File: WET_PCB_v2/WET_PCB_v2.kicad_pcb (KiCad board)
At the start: 2 copper layers, 100 x 80 mm, 185 parts, among them J1 Barrel jack, J10 POGO1, J11 Conn_01x09_Pin, J12 Conn_01x09_Pin, J13 Capacitor connector, J14 Capacitor connector, J15 Capacitor connector, J16 Capacitor connector, J17 Capacitor connector, J18 Capacitor connector, J2 Power input, J3 Jumper, J31 LA55_GND, J32 LA55_+, J33 LA55_M, J34 Capacitor connector, J35 PRGM_DBG, J36 LED_POWER, J37 PRGM_DBG, J39 TEST, J4 Coil plug, J40 TEST, J41 TEST, J43 PRGM_DBG, J44 GND, J45 PRGM_DBG, J46 GND, J47 GND, J5 Vsense_ADC1_IN1, J6 Pluggable Terminal Block, J7 Conn_01x09_Pin, J8 Conn_01x09_Pin, J9 POGO2, Q1 IRF530NPBF, Q2 IRF530NPBF, Q3 IRF530NPBF, Q4 IRF530NPBF, Q5 Q_NMOS_GDS, Q6 Q_NMOS_GDS, U1 Opamp_Quad, U3 IR2110, U4 IR2110, U5 IR2110, U6 L7805, U7 LA55-P

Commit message: small changes
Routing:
- net /decoration/UVLED1: track 247.3 -> 255.0 mm
- added copper zone on B.Cu, net /inverter/Vin_Inverter
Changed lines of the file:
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@@
 		(tags "Through hole socket strip THT 1x01 2.54mm single row")
 		(property "Reference" "J10"
-			(at -2.05 -0.114 0)
+			(at -2.22 -0.18 0)
 			(layer "F.SilkS")
 			(effects
@@
 		(tags "Diode SMF (DO-214AB)")
 		(property "Reference" "D11"
-			(at 3.188 -0.042 180)
+			(at 3.01 0 180)
 			(layer "F.SilkS")
 			(effects
@@
 		(tags "Through hole socket strip THT 1x01 2.54mm single row")
 		(property "Reference" "J9"
-			(at -0.17 2.64 0)
+			(at 2.47 0.35 0)
 			(layer "F.SilkS")
 			(effects
@@
 		(tags "C Radial series Radial pin pitch 2.00mm diameter 5mm height 11mm Non-Polar Electrolytic Capacitor")
 		(property "Reference" "C7"
-			(at 1 3.75 90)
+			(at 2.58 -3.16 90)
 			(layer "B.SilkS")
 			(effects
@@
 		(tags "C Rect series Radial pin pitch 5.00mm length 7mm width 2.5mm Capacitor")
 		(property "Reference" "C8"
-			(at 2.49 -0.35 90)
+			(at -2.36 0.01 90)
 			(layer "B.SilkS")
 			(effects
@@
 		(tags "phoenix_contact connector GMSTBA_01x02_G_7.62mm")
 		(property "Reference" "J6"
-			(at 3.81 3.2 90)
+			(at -3.005 3.32 90)
 			(layer "B.SilkS")
 			(effects
@@
 		(tags "resistor handsolder")
 		(property "Reference" "JMP12"
-			(at 0 1.65 90)
+			(at -1.32 -3.95 180)
 			(layer "B.SilkS")
 			(effects
@@
 	(gr_poly
 		(pts
-			(xy 174.725 114.375) (xy 173.001381 123.678195) (xy 173.048618 125.496805) (xy 175 125.5) (xy 175 123.225)
-			(xy 178.488164 117.139341) (xy 178.512424 114.408648)
-		)
-		(stroke
-			(width 0.2)
-			(type solid)
-		)
-		(fill yes)
-		(layer "B.Cu")
-		(net "/inverter/Vin_Inverter")
-	)
-	(gr_poly
-		(pts
 			(xy 181.075825 153.757093) (xy 181.084292 153.803897) (xy 181.105475 153.909778) (xy 181.128775 154.016543)
 			(xy 181.149937 154.105618) (xy 180.867124 154.15487) (xy 180.844361 154.142025) (xy 180.819374 154.126735)
@@
 	)
 	(segment
-		(start 200.5 81)
-		(end 201.5 82)
+		(start 166.56 157.02)
+		(end 164.75 155.21)
 		(width 0.2)
 		(layer "B.Cu")
@@
 	)
 	(segment
-		(start 165.25 106.25)
-		(end 161.5 102.5)
+		(start 200.5 81)
+		(end 201.5 82)
 		(width 0.2)
 		(layer "B.Cu")
@@
 	)
 	(segment
-		(start 166.56 157.02)
-		(end 164.75 155.21)
+		(start 183 155.25)
+		(end 185 153.25)
 		(width 0.2)
 		(layer "B.Cu")
@@
 	)
 	(segment
-		(start 183 155.25)
-		(end 185 153.25)
+		(start 181.23 157.02)
+		(end 166.56 157.02)
 		(width 0.2)
 		(layer "B.Cu")
@@
 	)
 	(segment
-		(start 169.25 136.25)
-		(end 165.25 132.25)
+		(start 174.06 140.64)
+		(end 174.06 139.46)
 		(width 0.2)
 		(layer "B.Cu")
@@
 	)
 	(segment
-		(start 169.25 140.75)
-		(end 169.25 136.25)
+		(start 183 158.75)
+		(end 183 155.25)
 		(width 0.2)
 		(layer "B.Cu")
@@
 	)
 	(segment
-		(start 183 158.75)
-		(end 183 155.25)
+		(start 257 152.75)
+		(end 257 156.25)
 		(width 0.2)
 		(layer "B.Cu")
@@
 	)
 	(segment
-		(start 257 152.75)
-		(end 257 156.25)
+		(start 164.75 145.25)
+		(end 167.81 142.19)
 		(width 0.2)
 		(layer "B.Cu")
@@
 	)
 	(segment
-		(start 164.75 155.21)
-		(end 164.75 145.25)
+		(start 172.03 137.43)
+		(end 170.43 137.43)
 		(width 0.2)
 		(layer "B.Cu")
@@
 	)
 	(segment
-		(start 165.25 132.25)
-		(end 165.25 106.25)
-		(width 0.2)
-		(layer "B.Cu")
-		(net "/decoration/UVLED1")
-	)
-	(segment
 		(start 185 153.25)
 		(end 181.23 157.02)
@@
 	)
 	(segment
-		(start 164.75 145.25)
-		(end 169.25 140.75)
+		(start 167.81 142.19)
+		(end 172.51 142.19)
 		(width 0.2)
 		(layer "B.Cu")
@@
 	)
 	(segment
+		(start 174.06 139.46)
+		(end 172.03 137.43)
+		(width 0.2)
+		(layer "B.Cu")
+		(net "/decoration/UVLED1")
+	)
+	(segment
+		(start 170.43 137.43)
+		(end 165.09 132.09)
+		(width 0.2)
+		(layer "B.Cu")
+		(net "/decoration/UVLED1")
+	)
+	(segment
 		(start 256.497057 152.25)
 		(end 256.5 152.25)
@@
 	)
 	(segment
+		(start 172.51 142.19)
+		(end 174.06 140.64)
+		(width 0.2)
+		(layer "B.Cu")
+		(net "/decoration/UVLED1")
+	)
+	(segment
 		(start 179.999285 84.5)
 		(end 183.499285 81)
@@
 	)
 	(segment
+		(start 165.09 132.09)
+		(end 165.09 106.09)
+		(width 0.2)
+		(layer "B.Cu")
+		(net "/decoration/UVLED1")
+	)
+	(segment
 		(start 255.027943 152.725)
 		(end 256.022057 152.725)
@@
 	)
 	(segment
+		(start 164.75 155.21)
+		(end 164.75 145.25)
+		(width 0.2)
+		(layer "B.Cu")
+		(net "/decoration/UVLED1")
+	)
+	(segment
 		(start 225.8 152.8)
 		(end 218.95 152.8)
@@
 	)
 	(segment
-		(start 181.23 157.02)
-		(end 166.56 157.02)
+		(start 165.09 106.09)
+		(end 161.5 102.5)
 		(width 0.2)
 		(layer "B.Cu")
@@
 				(xy 209.621576 151.526956) (xy 211.59981 151.573548) (xy 211.6 156.2) (xy 207.998583 157.18094)
 				(xy 180.5 157.5) (xy 179.33 156.99) (xy 175.277513 156.811356) (xy 168.006173 156.913797) (xy 159.114352 148.269036)
-				(xy 159 141.25)
+				(xy 158.86 141.08)
 			)
 		)
@@
 			)
 		)
+	)
+	(zone
+		(net "/inverter/Vin_Inverter")
+		(layer "B.Cu")
+		(hatch edge 0.5)
+		(priority 9)
+		(connect_pads yes
+			(clearance 0.5)
+		)
+		(min_thickness 0.25)
+		(fill yes
+			(thermal_gap 0.5)
+			(thermal_bridge_width 0.5)
+			(smoothing fillet)
+			(radius 2)
+			(island_removal_mode 0)
+		)
+		(polygon
+			(pts
+				(xy 174.44 114.16) (xy 173.001381 123.678195) (xy 173.048618 125.496805) (xy 175 125.5) (xy 175 123.225)
+				(xy 178.488164 117.139341) (xy 178.74 114.31)
+			)
+		)

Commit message: small changes
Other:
- board text added: "ryan"
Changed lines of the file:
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@@
+		)
+	)
+	(gr_text "ryan"
+		(at 198.83 144.97 0)
+		(layer "F.SilkS")
+		(effects
+			(font
+				(face "Comic Sans MS")
+				(size 0.5 0.5)
+				(thickness 0.1)
+			)
+			(justify left bottom)
+		)
+		(render_cache "ryan" 0
+			(polygon
+				(pts
+					(xy 199.14321 144.633185) (xy 199.139618 144.653636) (xy 199.132646 144.666239) (xy 199.122759 144.673403)
+					(xy 199.109047 144.675928) (xy 199.096049 144.673768) (xy 199.08735 144.667887) (xy 199.081811 144.657976)
+					(xy 199.079677 144.642283) (xy 199.078669 144.6185) (xy 199.077631 144.589954) (xy 199.042358 144.596652)
+					(xy 199.013954 144.606913) (xy 198.99123 144.620301) (xy 198.972863 144.636744) (xy 198.955996 144.658681)
+					(xy 198.940672 144.687132) (xy 198.941344 144.874009) (xy 198.939012 144.889718) (xy 198.932837 144.899888)
+					(xy 198.92284 144.906111) (xy 198.907516 144.908447) (xy 198.894233 144.906233) (xy 198.885334 144.900199)
+					(xy 198.879661 144.890019) (xy 198.877474 144.873886) (xy 198.877474 144.633643) (xy 198.878329 144.599785)
+					(xy 198.879184 144.565896) (xy 198.881371 144.549763) (xy 198.887044 144.539583) (xy 198.895942 144.53355)
+					(xy 198.909226 144.531336) (xy 198.922812 144.534366) (xy 198.932857 144.543351) (xy 198.940003 144.560256)
+					(xy 198.943053 144.589252) (xy 198.970946 144.565487) (xy 198.999179 144.547707) (xy 199.027977 144.535316)
+					(xy 199.057646 144.527946) (xy 199.088561 144.525474) (xy 199.105876 144.527924) (xy 199.119327 144.534828)
+					(xy 199.129869 144.546326) (xy 199.136912 144.560942) (xy 199.14172 144.58134) (xy 199.143546 144.609249)
+				)
+			)
+			(polygon
+				(pts
+					(xy 199.511407 144.58049) (xy 199.393224 144.835876) (xy 199.352867 144.925617) (xy 199.32627 144.991917)
+					(xy 199.303739 145.058168) (xy 199.295962 145.072095) (xy 199.285934 145.079749) (xy 199.272995 145.082348)
+					(xy 199.259585 145.079998) (xy 199.248204 145.073005) (xy 199.240394 145.062536) (xy 199.237793 145.049772)
+					(xy 199.242228 145.025404) (xy 199.262433 144.967638) (xy 199.311585 144.853401) (xy 199.189311 144.617096)
+					(xy 199.173924 144.592061) (xy 199.166688 144.576619) (xy 199.164704 144.565652) (xy 199.16733 144.552973)
+					(xy 199.17545 144.541686) (xy 199.187041 144.533847) (xy 199.199539 144.531336) (xy 199.213656 144.534193)
+					(xy 199.223811 144.542418) (xy 199.260021 144.598229) (xy 199.301381 144.673785) (xy 199.348466 144.773167)
+					(xy 199.399024 144.654129) (xy 199.426735 144.595604) (xy 199.451628 144.548891) (xy 199.460147 144.537596)
+					(xy 199.469564 144.531416) (xy 199.480327 144.529382) (xy 199.493422 144.531854) (xy 199.505056 144.539396)
+					(xy 199.513184 144.550455) (xy 199.515833 144.56321) (xy 199.514822 144.570952)
+				)
+			)
+			(polygon
+				(pts
+					(xy 199.770301 144.530978) (xy 199.806666 144.542785) (xy 199.829633 144.554505) (xy 199.843492 144.565976)
+					(xy 199.850801 144.57727) (xy 199.853102 144.588886) (xy 199.851431 144.59752) (xy 199.846294 144.60528)
+					(xy 199.840982 144.647992) (xy 199.838784 144.724135) (xy 199.840253 144.764265) (xy 199.844584 144.791058)
+					(xy 199.850265 144.809607) (xy 199.866108 144.851172) (xy 199.873954 144.869276) (xy 199.876 144.875077)
+					(xy 199.873583 144.887599) (xy 199.866444 144.897609) (xy 199.856072 144.90429) (xy 199.844248 144.906493)
+					(xy 199.836953 144.903919) (xy 199.820679 144.891808) (xy 199.806584 144.87813) (xy 199.797781 144.867414)
+					(xy 199.765688 144.883276) (xy 199.740048 144.893701) (xy 199.715923 144.900626) (xy 199.698405 144.902585)
+					(xy 199.658515 144.899317) (xy 199.626839 144.890322) (xy 199.601716 144.876351) (xy 199.581932 144.857492)
+					(xy 199.56796 144.835758) (xy 199.557171 144.807861) (xy 199.550047 144.772387) (xy 199.547589 144.730333)
+					(xy 199.614721 144.730333) (xy 199.617338 144.767233) (xy 199.62427 144.794414) (xy 199.634535 144.814108)
+					(xy 199.64964 144.829393) (xy 199.668994 144.838692) (xy 199.693978 144.842013) (xy 199.725137 144.838851)
+					(xy 199.749635 144.830106) (xy 199.762802 144.821593) (xy 199.784134 144.804216) (xy 199.775488 144.719598)
+					(xy 199.773204 144.669028) (xy 199.775067 144.637215) (xy 199.780715 144.600609) (xy 199.759008 144.591084)
+					(xy 199.744506 144.588) (xy 199.719081 144.590662) (xy 199.69571 144.598527) (xy 199.673846 144.61178)
+					(xy 199.653128 144.631079) (xy 199.636133 144.653747) (xy 199.624257 144.677602) (xy 199.617137 144.702981)
+					(xy 199.614721 144.730333) (xy 199.547589 144.730333) (xy 199.547432 144.727646) (xy 199.551066 144.687366)
+					(xy 199.561685 144.650846) (xy 199.579257 144.617309) (xy 199.60428 144.586199) (xy 199.634627 144.560113)
+					(xy 199.666982 144.541985) (xy 199.701878 144.531125) (xy 199.740079 144.527428)
+				)
+			)
+			(polygon
+				(pts
+					(xy 200.197515 144.908447) (xy 200.184248 144.906375) (xy 200.1748 144.900658) (xy 200.168179 144.891097)
+					(xy 200.16439 144.876329) (xy 200.154834 144.80153) (xy 200.151193 144.762108) (xy 200.15004 144.7267)
+					(xy 200.151231 144.694246) (xy 200.152422 144.661792) (xy 200.149667 144.622371) (xy 200.143265 144.601086)
+					(xy 200.135058 144.591036) (xy 200.125097 144.588) (xy 200.107447 144.590469) (xy 200.089703 144.598147)
+					(xy 200.07134 144.611957) (xy 200.052008 144.633429) (xy 200.033272 144.66219) (xy 200.016802 144.696755)
+					(xy 200.002823 144.737996) (xy 199.99974 144.771488) (xy 199.997694 144.804613) (xy 199.99974 144.835388)
+					(xy 200.001785 144.866132) (xy 199.999351 144.880257) (xy 199.992382 144.891045) (xy 199.981823 144.898178)
+					(xy 199.968324 144.900631) (xy 199.954554 144.898166) (xy 199.944052 144.891075) (xy 199.937223 144.880307)
+					(xy 199.934832 144.866193) (xy 199.932603 144.835479) (xy 199.930405 144.804796) (xy 199.935351 144.707404)
+					(xy 199.940327 144.610043) (xy 199.939106 144.57762) (xy 199.937916 144.545227) (xy 199.940403 144.531741)
+					(xy 199.947655 144.521169) (xy 199.958454 144.514176) (xy 199.971743 144.511796) (xy 199.985199 144.514347)
+					(xy 199.995101 144.521668) (xy 200.002275 144.534702) (xy 200.006212 144.556004) (xy 200.00725 144.595816)
+					(xy 200.033035 144.565584) (xy 200.057376 144.544223) (xy 200.080552 144.530154) (xy 200.102958 144.522191)
+					(xy 200.125097 144.519612) (xy 200.15104 144.522799) (xy 200.171663 144.531759) (xy 200.188222 144.5464)
+					(xy 200.20127 144.567698) (xy 200.208881 144.589685) (xy 200.214517 144.620495) (xy 200.217329 144.662525)
+					(xy 200.217329 144.696963) (xy 200.216994 144.728684) (xy 200.218612 144.75896) (xy 200.224321 144.801865)
+					(xy 200.230059 144.844724) (xy 200.231679 144.87468) (xy 200.229177 144.888456) (xy 200.221939 144.899074)
+					(xy 200.211094 144.906053)
+				)
+			)
 		)
 	)

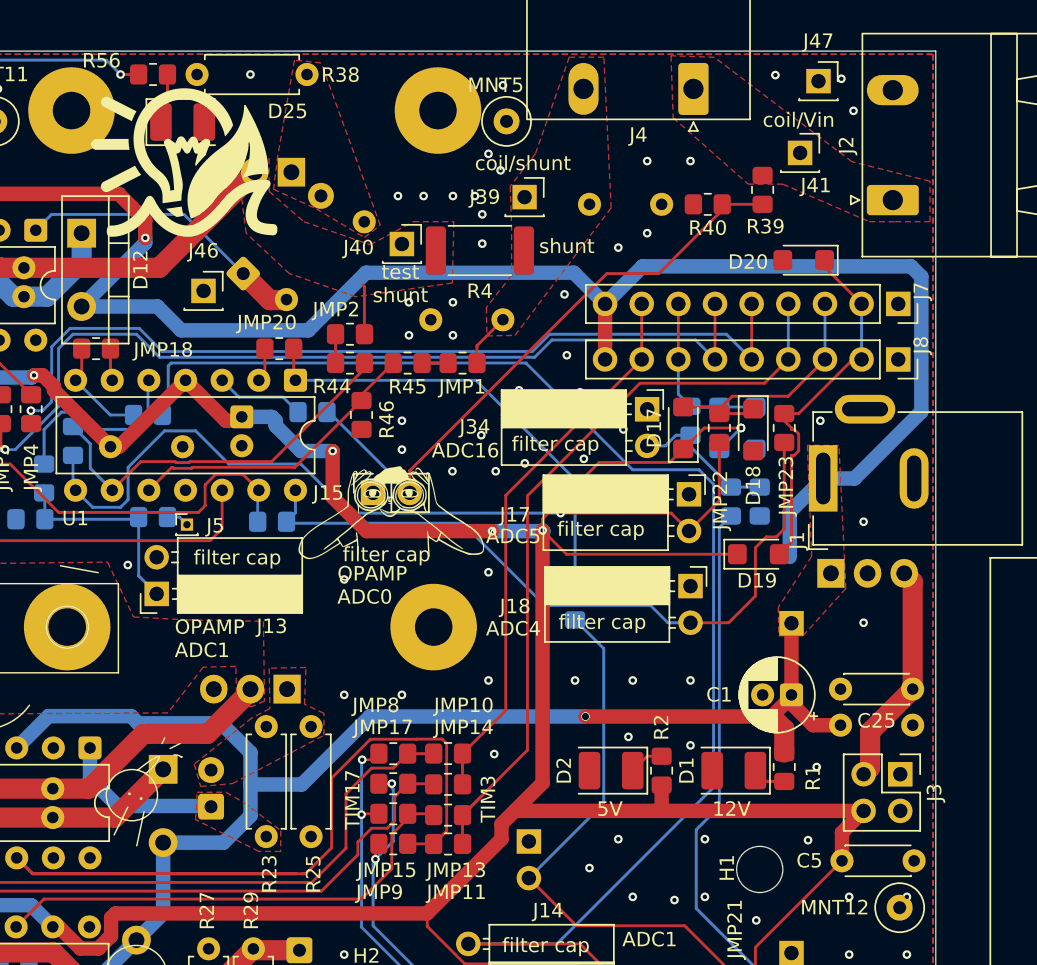
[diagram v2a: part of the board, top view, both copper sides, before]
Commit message: cleaned up schematics, added power LED
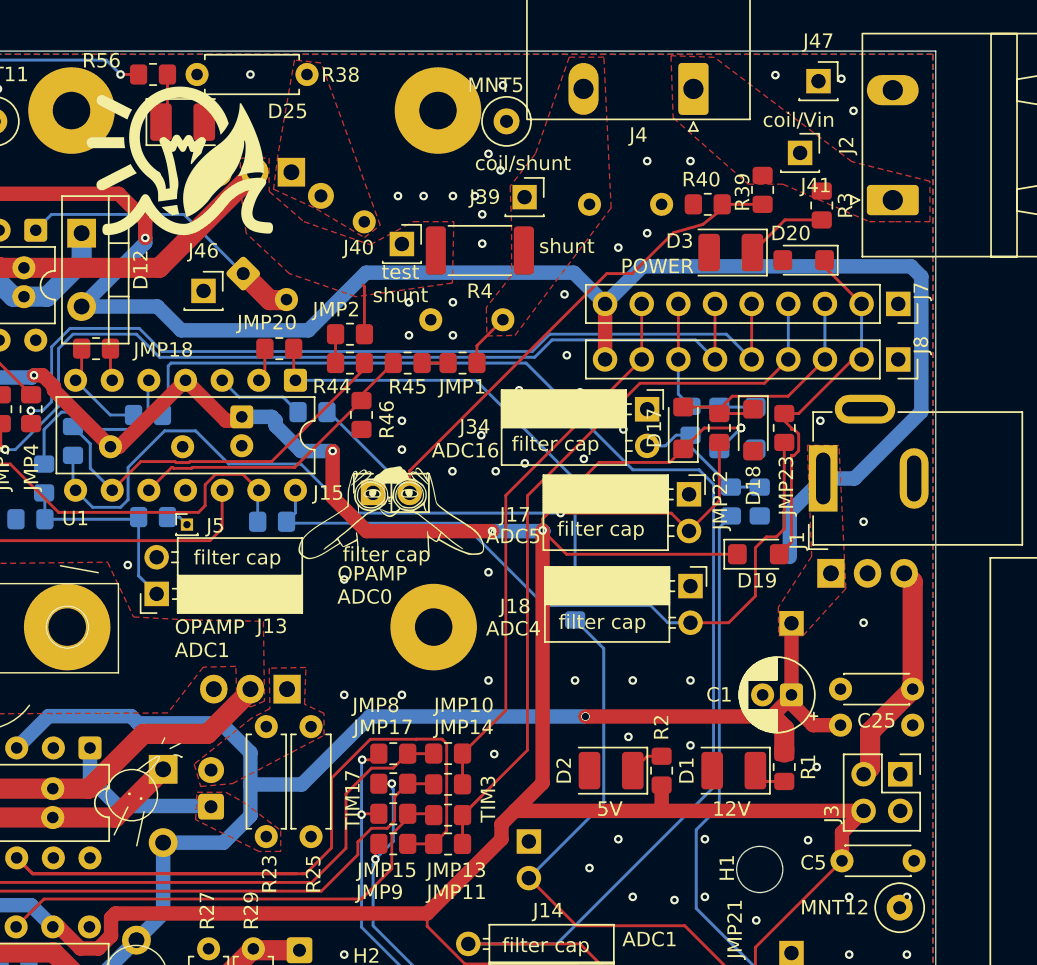
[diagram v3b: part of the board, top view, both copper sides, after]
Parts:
- added D3: LED, LED_SMD:LED_PLCC-2_3.4x3.0mm_AK, F.Cu at (243.8, 94.3)
- added R3: R, Resistor_SMD:R_0805_2012Metric_Pad1.20x1.40mm_HandSolder, F.Cu at (250.1, 91.1)
- J43, J45: value PRGM_DBG -> TEST
- J6: value Pluggable Terminal Block -> TX Coil out
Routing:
- net Net-(D3-A): track 0.00 -> 5.74 mm
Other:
- board text added: "NRST_EXT_SYS_NRST PB7_EXT_TIM17_CH1N PC14_EXT_TIM17_CH1 PC15_EXT_GPIO_PC15 PA0_EXT_ADC1_IN0 PA1_EXT_ADC_IN1 PA2_EXT_USART2_TX PA3_EXT_USART2_RX GND"
- board text added: "POWER"
- board text added: "Raf van Mil, Jake Voets, Lara Korink Romani, Joshua van Sandijk, Fintan Rising, Radman Mustafa, Oliwia Hejduk, Max Schraven"
- board text added: "VDD PB3_EXT_GPIO_PB3 PA12_EXT_GPIO_PA12 PB0_EXT_TIM1_CH1 PA7_EXT_TIM1_CH1N PA5_EXT_ADC1_IN5 PA4_EXT_ADC1_IN4 GND"
- board text removed: "Raf van Mil, Jake Voets, Oliwia Hejduk, Radman Mustafa, Joshua van Sandijk, Fintan Rising, Lara Korink Romani, Max Schraven"

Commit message: added missing caps
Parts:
- added C26: C322C104K5R5TA, Capacitor_THT:C_Disc_D4.3mm_W1.9mm_P5.00mm, F.Cu at (193.8, 88.5)
- added C27: MCGPR63V106M5X11, Capacitor_THT:C_Radial_D5.0mm_H11.0mm_P2.00mm, F.Cu at (204.2, 98.0)
- added C28: C322C104K5R5TA, Capacitor_THT:C_Disc_D4.3mm_W1.9mm_P5.00mm, B.Cu at (189.5, 134.1)
- added C29: MCGPR63V106M5X11, Capacitor_THT:C_Radial_D5.0mm_H11.0mm_P2.00mm, B.Cu at (214.2, 131.2)
- added C30: C322C104K5R5TA, Capacitor_THT:C_Disc_D4.3mm_W1.9mm_P5.00mm, B.Cu at (181.0, 145.6)
- added C31: MCGPR63V106M5X11, Capacitor_THT:C_Radial_D5.0mm_H11.0mm_P2.00mm, B.Cu at (207.4, 147.0)
- J3: value Jumper -> 5v source select
- moved J44 66.1 mm to (230.0, 130.0)
- moved J46 42.3 mm to (165.0, 95.0)
- moved J47 38.4 mm to (211.5, 84.5)
- moved C12 3.16 mm to (190.3, 144.6), turned to -135 degrees
- moved C7 2.84 mm to (198.8, 133.5), turned to 90 degrees
- moved JMP12 1.73 mm to (193.5, 134.0), turned to 0 degrees
- moved C6 0.79 mm to (189.3, 131.0)
- moved C23 0.42 mm to (194.5, 95.1)
- moved C22 0.23 mm to (180.0, 95.5)
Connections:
- C12 pad 1: /inverter/Vout_Inverter_- -> Net-(C12-+)
- C12 pad 2: Net-(C12--) -> /inverter/Vout_Inverter_-
- C13 pad 2: Net-(C12--) -> Net-(C12-+)
- C22 pad 2: Net-(C23--) -> Net-(C23-+)
- C23 pad 1: /DCDC/currsense_FET_side -> Net-(C23-+)
- C23 pad 2: Net-(C23--) -> /DCDC/currsense_FET_side
- C6 pad 2: Net-(C7--) -> Net-(C7-+)
- C7 pad 1: /inverter/Vout_Inverter_+ -> Net-(C7-+)
- C7 pad 2: Net-(C7--) -> /inverter/Vout_Inverter_+
- D12 pad 1: Net-(C23--) -> Net-(C23-+)
- D4 pad 1: Net-(C7--) -> Net-(C7-+)
- D9 pad 1: Net-(C12--) -> Net-(C12-+)
- U3 pad 6: Net-(C7--) -> Net-(C7-+)
- U4 pad 6: Net-(C12--) -> Net-(C12-+)
- U5 pad 6: Net-(C23--) -> Net-(C23-+)
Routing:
- net Net-(C7--): track 26.8 -> 0.00 mm
- net Net-(C7-+): track 0.00 -> 26.7 mm
- net Net-(C23--): track 21.9 -> 0.00 mm
- net Net-(C23-+): track 0.00 -> 21.1 mm
- net Net-(C12--): track 18.6 -> 0.00 mm
- net Net-(C12-+): track 0.00 -> 16.1 mm
- net +12V: track 219.9 -> 235.6 mm
- net /TIM1_CH4: track 62.4 -> 60.7 mm
- net /TIM14_CH1: track 61.2 -> 59.8 mm
- net Net-(D6-K): track 11.3 -> 10.1 mm
- net /inverter/Vout_Inverter_+: track 26.5 -> 27.5 mm
- net /inverter/Vout_Inverter_-: track 11.6 -> 10.8 mm
- net /DCDC/currsense_FET_side: track 76.1 -> 75.9 mm, vias 1 -> 0
- net GND: vias 107 -> 106
